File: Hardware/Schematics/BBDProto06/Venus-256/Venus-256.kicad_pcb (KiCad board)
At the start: 4 copper layers, 172.7 x 109.2 mm, 231 parts, among them J201 RaspberryPi header, J301 ARM JTAG, U1001 AD7616, U101 TPS22993, U401 AD7616, U501 ATSAME70Q21A-AN, U601 AD7616, U701 AD7616, U801 AD7616, U901 ATSAME70Q21A-AN

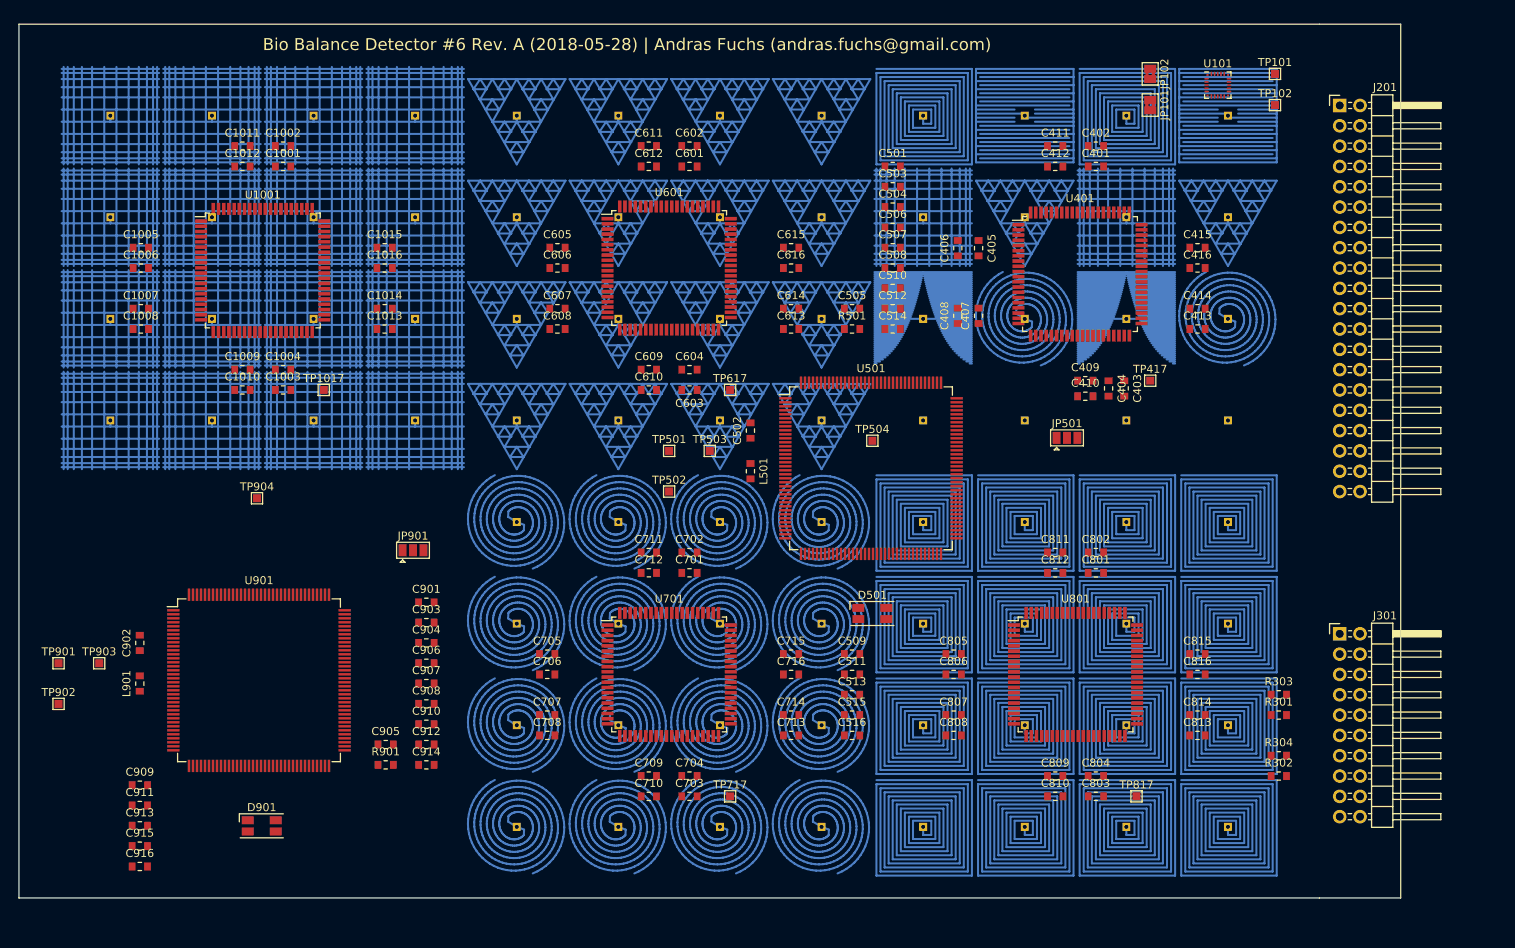
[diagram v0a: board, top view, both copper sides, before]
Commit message: Expanded the sensors by adding an extra 0.65mm gap between them and rearraged the MCUs a little
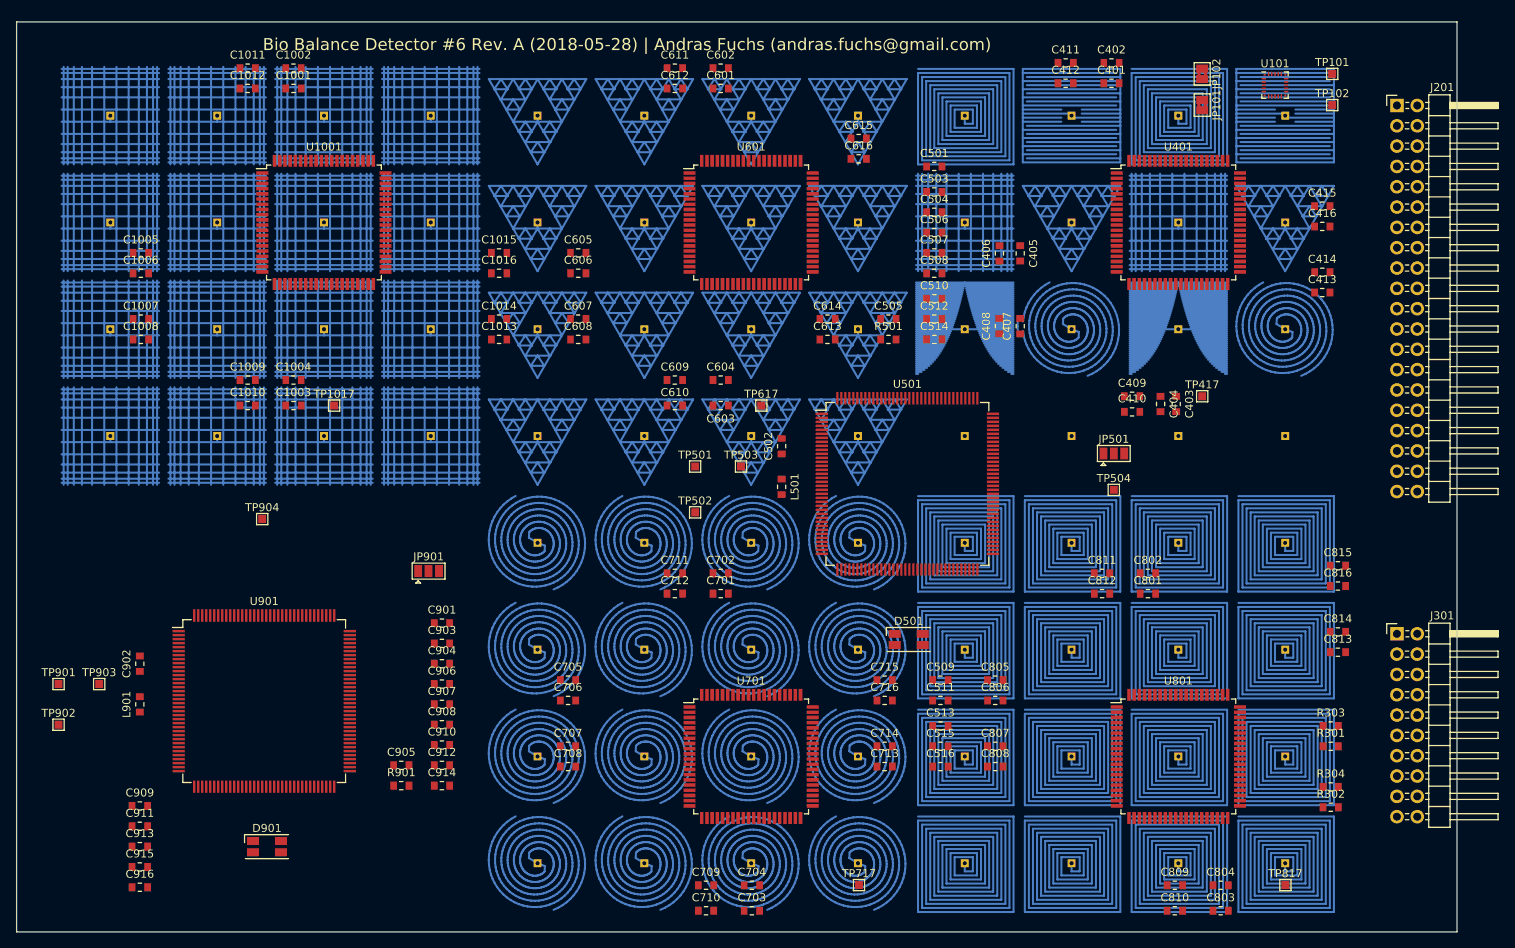
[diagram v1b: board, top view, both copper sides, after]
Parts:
- moved TP504 30.8 mm to (152.1, 73.5)
- moved TP817 21.7 mm to (173.6, 122.8)
- moved C803 21.2 mm to (165.5, 126.1)
- moved C815 20.7 mm to (180.1, 82.9)
- moved C816 20.7 mm to (180.1, 85.5)
- moved C804 20.7 mm to (165.5, 122.9)
- moved C810 20.7 mm to (159.7, 126.1)
- moved C813 20.4 mm to (180.1, 93.7)
- moved C814 20.4 mm to (180.1, 91.2)
- moved C809 20.2 mm to (159.7, 122.9)
- moved TP717 19.6 mm to (120.2, 122.8)
- moved C415 16.4 mm to (178.2, 38.0)
- moved C416 16.4 mm to (178.2, 40.5)
- moved U801 16.4 mm to (160.2, 106.8)
- moved C703 16.3 mm to (106.9, 126.1)
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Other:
- board size 172.7 x 109.2 mm -> 180.1 x 113.7 mm

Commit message: Rearranged the MCUs a little more to make the routing easier
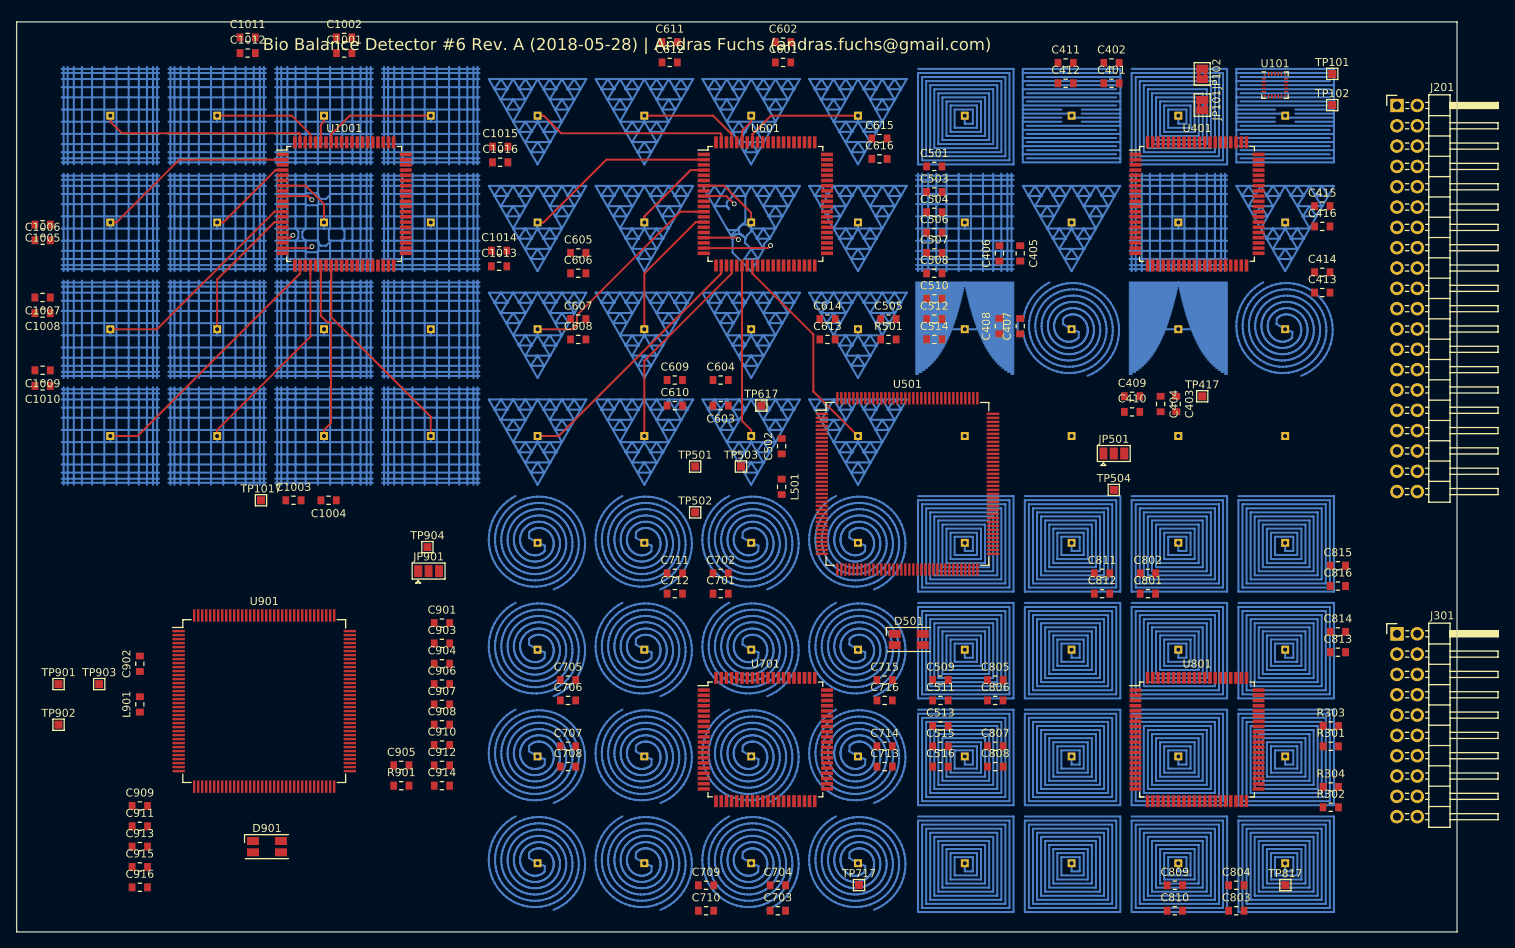
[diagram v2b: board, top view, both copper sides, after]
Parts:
- moved C1010 25.7 mm to (18.2, 60.5), turned to 180 degrees
- moved C1009 25.7 mm to (18.2, 58.5), turned to 180 degrees
- moved TP904 20.9 mm to (66.3, 80.6)
- moved C1004 15.7 mm to (54.0, 74.8), turned to 180 degrees
- moved TP1017 15.0 mm to (45.5, 74.8)
- moved C1016 13.9 mm to (75.4, 32.5)
- moved C1015 13.3 mm to (75.4, 30.6)
- moved C1006 13.0 mm to (18.2, 42.2)
- moved C1005 12.8 mm to (18.2, 40.3), turned to 180 degrees
- moved C1008 12.7 mm to (18.2, 51.4), turned to 180 degrees
- moved C1007 12.6 mm to (18.2, 49.4), turned to 180 degrees
- moved C1003 11.8 mm to (49.6, 74.8)
- moved C1013 9.14 mm to (75.3, 45.5)
- moved C1014 8.55 mm to (75.3, 43.5)
- moved C601 8.45 mm to (110.8, 20.0)
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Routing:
- net Net-(TP1016-Pad1): track 293.4 -> 326.5 mm
- net Net-(TP616-Pad1): track 125.8 -> 158.2 mm
- net Net-(TP612-Pad1): track 125.8 -> 153.5 mm
- net Net-(TP1012-Pad1): track 293.4 -> 321.0 mm
- net Net-(TP613-Pad1): track 125.8 -> 152.6 mm
- net Net-(TP1013-Pad1): track 293.4 -> 319.8 mm
- net Net-(TP1015-Pad1): track 293.4 -> 319.5 mm
- net Net-(TP1004-Pad1): track 293.4 -> 319.5 mm
- net Net-(TP615-Pad1): track 125.8 -> 151.7 mm
- net Net-(TP604-Pad1): track 125.8 -> 150.8 mm
- net Net-(TP1008-Pad1): track 293.4 -> 318.1 mm
- net Net-(TP609-Pad1): track 125.8 -> 150.0 mm, vias 0 -> 1
- net Net-(TP608-Pad1): track 125.8 -> 149.9 mm
- net Net-(TP1009-Pad1): track 293.4 -> 316.3 mm, vias 0 -> 1
- net Net-(TP1014-Pad1): track 293.4 -> 315.8 mm
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
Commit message: Connected the sensors manually
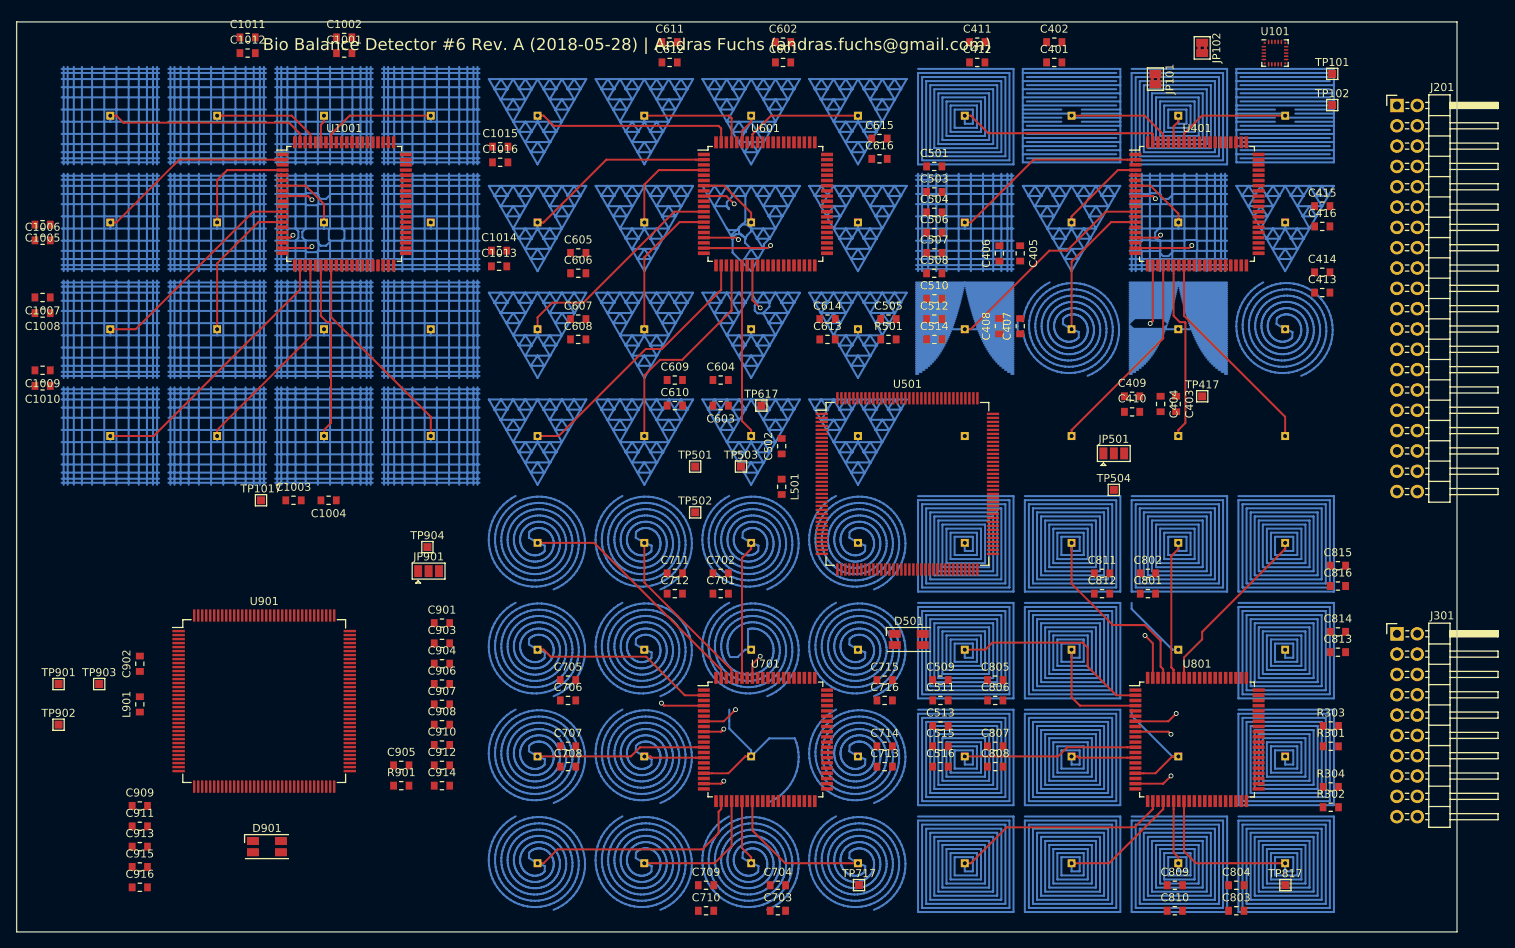
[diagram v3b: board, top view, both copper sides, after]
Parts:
- moved C411 11.4 mm to (135.0, 17.5)
- moved C412 11.4 mm to (135.0, 20.0)
- moved C401 7.61 mm to (144.7, 20.0)
- moved C402 7.61 mm to (144.7, 17.5)
- moved JP101 6.69 mm to (157.3, 22.1)
- moved U101 4.01 mm to (172.2, 18.9)
- moved JP102 3.25 mm to (163.2, 18.2)
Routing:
- net Net-(TP810-Pad1): track 300.2 -> 14.9 mm
- net Net-(TP806-Pad1): track 300.2 -> 22.3 mm, vias 0 -> 1
- net Net-(TP710-Pad1): track 154.0 -> 30.0 mm
- net Net-(TP416-Pad1): track 0.00 -> 36.4 mm, vias 0 -> 1
- net Net-(TP804-Pad1): track 300.2 -> 333.3 mm, vias 0 -> 1
- net Net-(TP704-Pad1): track 154.0 -> 184.5 mm
- net Net-(TP716-Pad1): track 154.0 -> 182.3 mm
- net Net-(TP412-Pad1): track 384.1 -> 411.5 mm
- net Net-(TP816-Pad1): track 300.2 -> 327.5 mm
- net Net-(TP413-Pad1): track 0.00 -> 26.6 mm
- net Net-(TP415-Pad1): track 0.00 -> 26.1 mm
- net Net-(TP808-Pad1): track 300.2 -> 326.0 mm
- net Net-(TP404-Pad1): track 300.2 -> 325.7 mm
- net Net-(TP408-Pad1): track 293.4 -> 317.9 mm
- net Net-(TP803-Pad1): track 300.2 -> 324.2 mm
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
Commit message: Revert "Connected the sensors manually"
This reverts commit 920ffef15f235d024d89dcae21abf078b3e216eb.
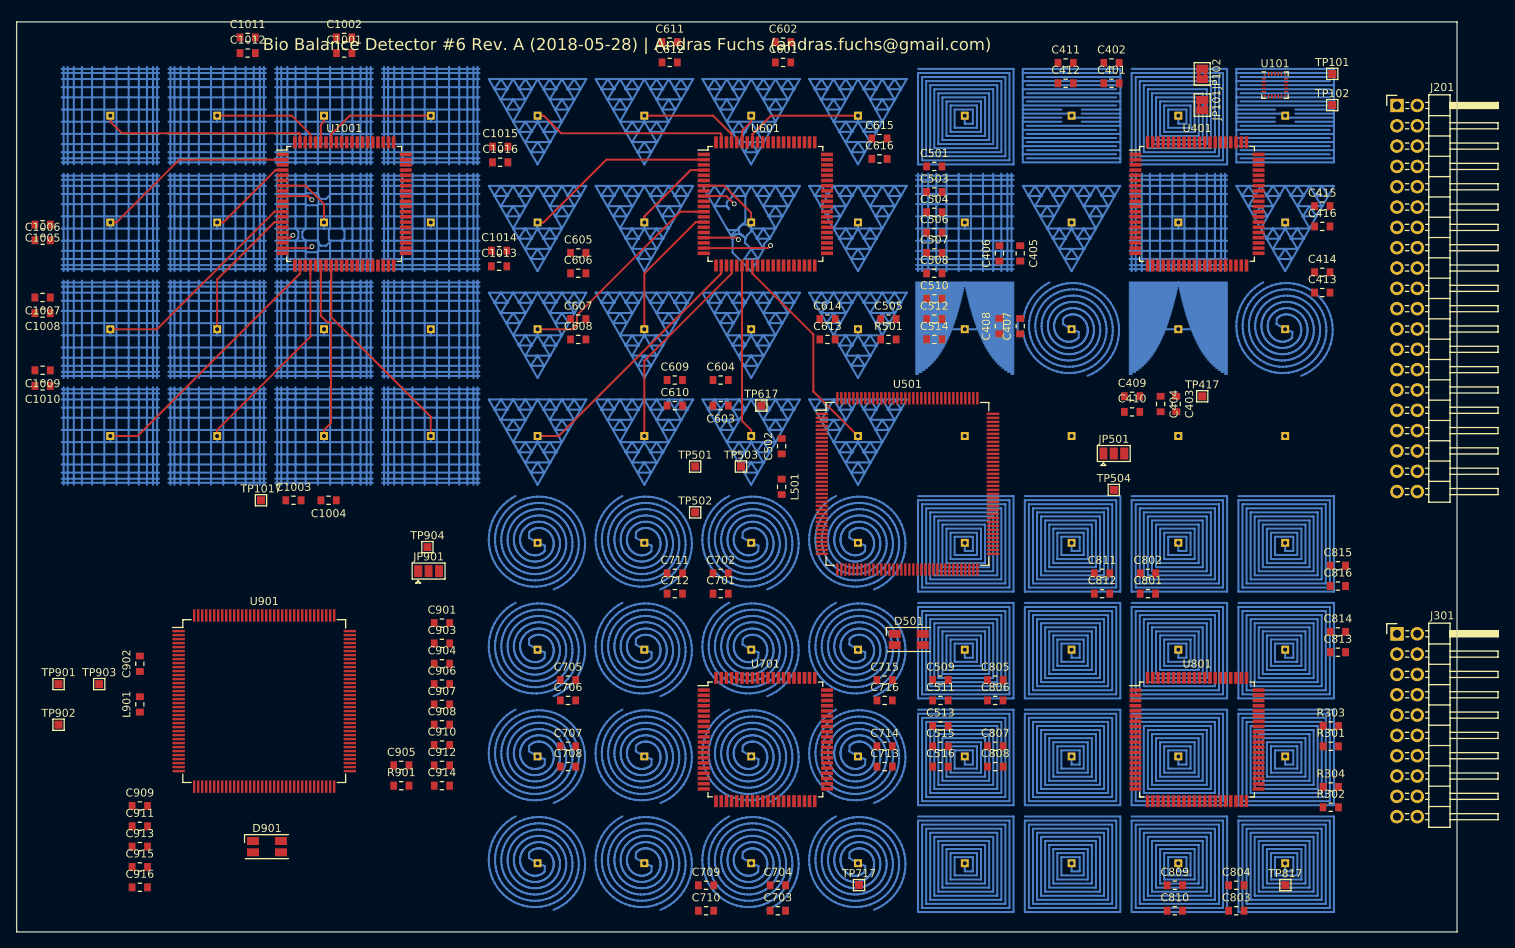
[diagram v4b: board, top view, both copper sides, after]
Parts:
- moved C411 11.4 mm to (146.1, 20.1)
- moved C412 11.4 mm to (146.1, 22.6)
- moved C401 7.61 mm to (151.8, 22.6)
- moved C402 7.61 mm to (151.8, 20.1)
- moved JP101 6.69 mm to (163.2, 25.4)
- moved U101 4.01 mm to (172.2, 22.9)
- moved JP102 3.25 mm to (163.2, 21.4)
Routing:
- net Net-(TP810-Pad1): track 14.9 -> 300.2 mm
- net Net-(TP806-Pad1): track 22.3 -> 300.2 mm, vias 1 -> 0
- net Net-(TP710-Pad1): track 30.0 -> 154.0 mm
- net Net-(TP416-Pad1): track 36.4 -> 0.00 mm, vias 1 -> 0
- net Net-(TP804-Pad1): track 333.3 -> 300.2 mm, vias 1 -> 0
- net Net-(TP704-Pad1): track 184.5 -> 154.0 mm
- net Net-(TP716-Pad1): track 182.3 -> 154.0 mm
- net Net-(TP412-Pad1): track 411.5 -> 384.1 mm
- net Net-(TP816-Pad1): track 327.5 -> 300.2 mm
- net Net-(TP413-Pad1): track 26.6 -> 0.00 mm
- net Net-(TP415-Pad1): track 26.1 -> 0.00 mm
- net Net-(TP808-Pad1): track 326.0 -> 300.2 mm
- net Net-(TP404-Pad1): track 325.7 -> 300.2 mm
- net Net-(TP408-Pad1): track 317.9 -> 293.4 mm
- net Net-(TP803-Pad1): track 324.2 -> 300.2 mm
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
